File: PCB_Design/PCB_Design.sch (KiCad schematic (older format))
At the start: 14 parts

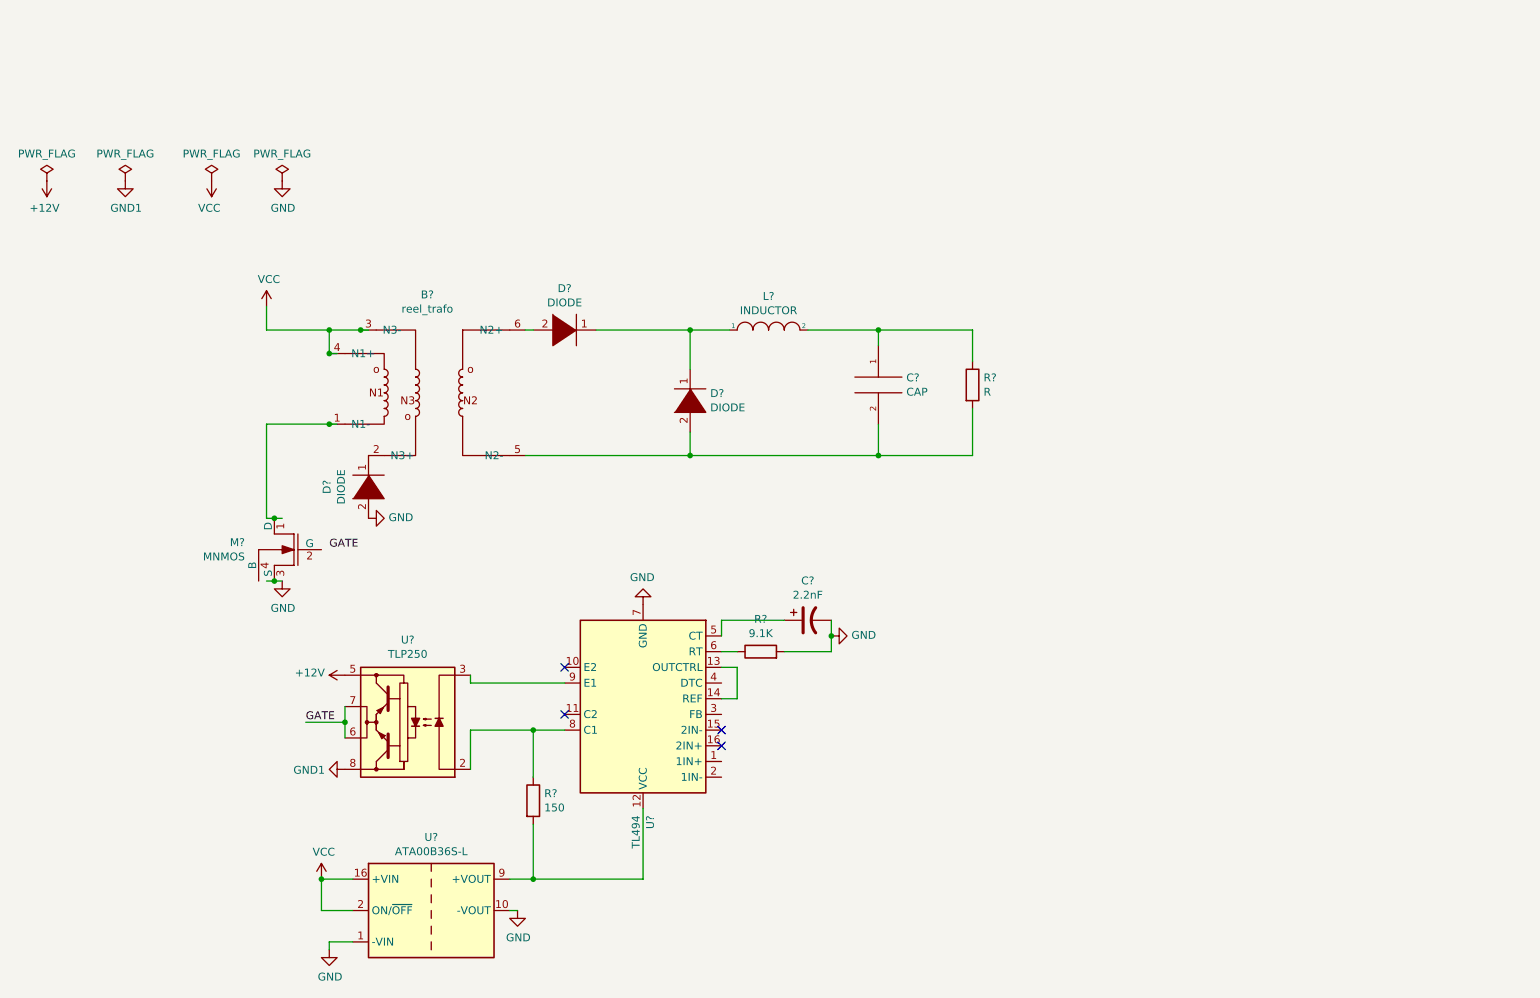
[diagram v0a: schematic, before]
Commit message: schematic and footprint assoc are done
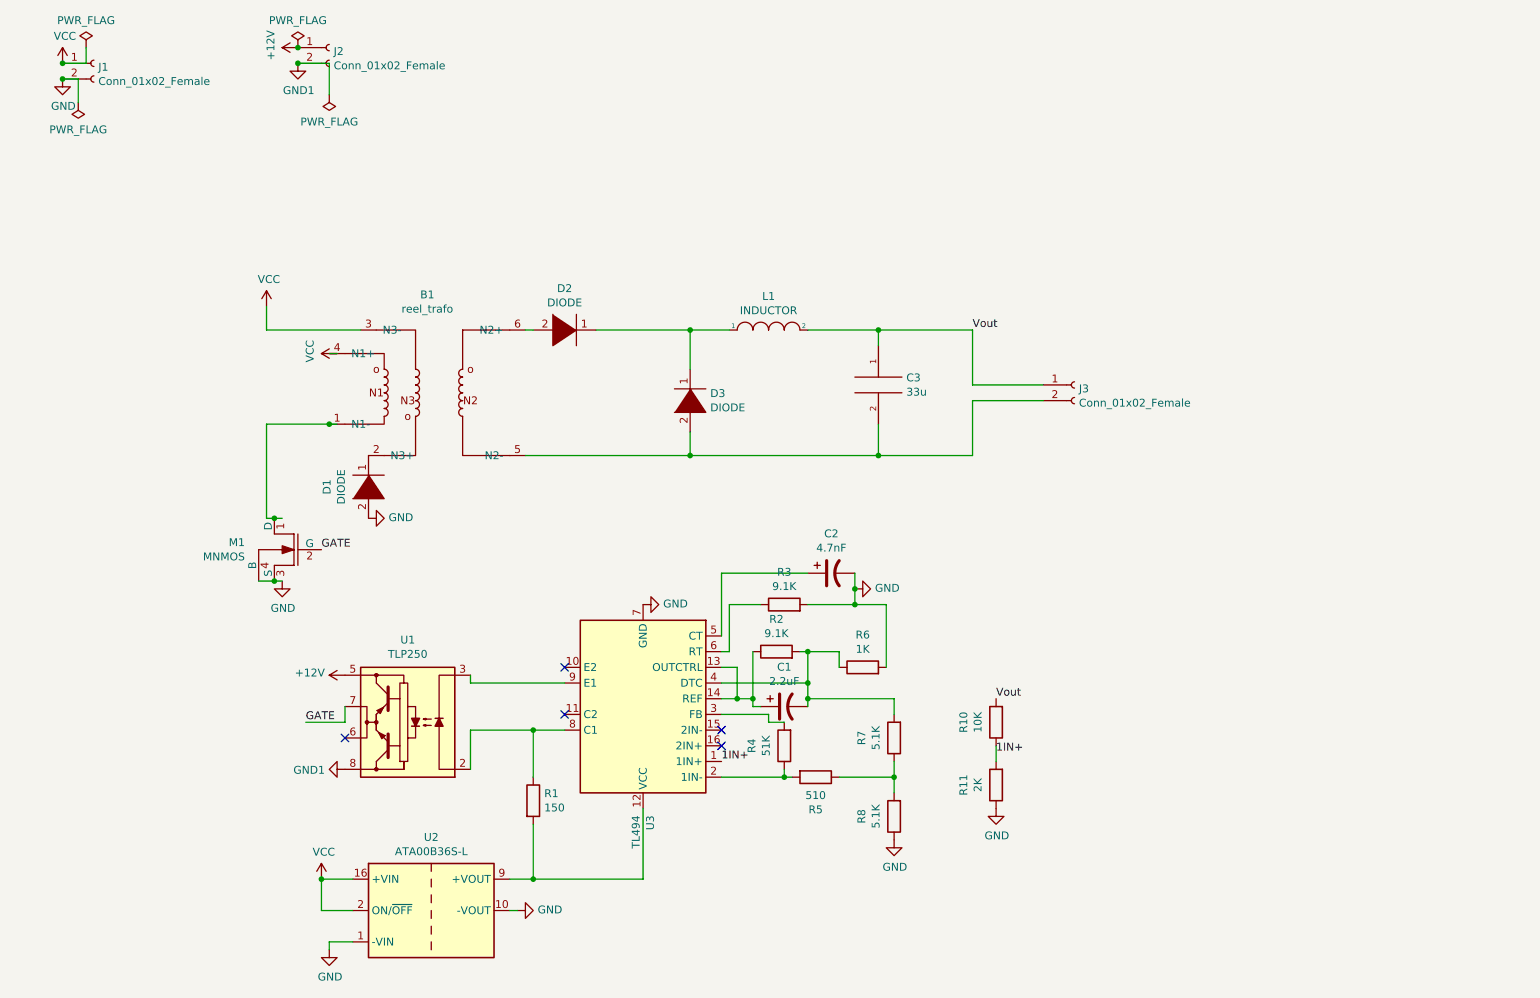
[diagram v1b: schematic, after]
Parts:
- removed R?: R, symbol Device:R
- added C1: 2.2uF, symbol Device:CP1
- added J1, J2, J3: Conn_01x02_Female, symbol Connector:Conn_01x02_Female
- added R10: 10K, Resistor_SMD:R_2512_6332Metric, symbol Device:R
- added R11: 2K, Resistor_SMD:R_2512_6332Metric, symbol Device:R
- added R2: 9.1K, Resistor_SMD:R_2512_6332Metric, symbol Device:R
- added R4: 51K, Resistor_SMD:R_2512_6332Metric, symbol Device:R
- added R5: 510, Resistor_SMD:R_2512_6332Metric, symbol Device:R
- added R6: 1K, Resistor_SMD:R_2512_6332Metric, symbol Device:R
- added R7, R8: 5.1K, Resistor_SMD:R_2512_6332Metric, symbol Device:R
- C2: renamed from C?; value 2.2nF -> 4.7nF
- C3: renamed from C?; value CAP -> 33u; footprint (none) -> Capacitor_SMD:C_1206_3216Metric_Pad1.42x1.75mm_HandSolder
- R1, R3: renamed from R?; footprint (none) -> Resistor_SMD:R_2512_6332Metric
- U3: renamed from U?; footprint (none) -> Package_DIP:DIP-16_W7.62mm
- gave numbers to parts that had none: 8
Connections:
- net labels added: 1IN+, Vout
- wire segments 55 -> 86
- no-connect marks 4 -> 5
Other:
- moved on the sheet: C2, R3

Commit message: started layout
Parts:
- removed J3: Conn_01x02_Female, symbol Connector:Conn_01x02_Female
- added J3: Conn_01x02_Male, Connector:Banana_Jack_2Pin, symbol Connector:Conn_01x02_Male
- B1: footprint (none) -> Transformer_THT:trafo
- C1, C2: footprint (none) -> Capacitor_SMD:C_1206_3216Metric_Pad1.42x1.75mm_HandSolder
- D1, D2, D3: footprint (none) -> Package_TO_SOT_THT:TO-220-2_Vertical
- J1, J2: footprint (none) -> Connector:Banana_Jack_2Pin
- L1: footprint (none) -> Inductor_THT:L_Toroid_Horizontal_D32.5mm_P28.90mm_Bourns_2300
- M1: footprint (none) -> Package_TO_SOT_THT:TO-220-3_Vertical
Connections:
- net Vout: now also J3.2 (Pin_2)
- net at B1.5 (N2-), C3.2, D3.2 (K): now also J3.1 (Pin_1)
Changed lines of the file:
@@
 F 0 "D1" H 3300 4065 50  0000 C CNN
 F 1 "DIODE" H 3300 3974 50  0000 C CNN
-F 2 "" H 3300 3800 50  0001 C CNN
+F 2 "Package_TO_SOT_THT:TO-220-2_Vertical" H 3300 3800 50  0001 C CNN
 F 3 "~" H 3300 3800 50  0001 C CNN
 	1    3300 3800
@@
 F 0 "D2" H 4550 3065 50  0000 C CNN
 F 1 "DIODE" H 4550 2974 50  0000 C CNN
-F 2 "" H 4550 2800 50  0001 C CNN
+F 2 "Package_TO_SOT_THT:TO-220-2_Vertical" H 4550 2800 50  0001 C CNN
 F 3 "~" H 4550 2800 50  0001 C CNN
 	1    4550 2800
@@
 F 0 "D3" V 5396 3122 50  0000 R CNN
 F 1 "DIODE" V 5305 3122 50  0000 R CNN
-F 2 "" H 5350 3250 50  0001 C CNN
+F 2 "Package_TO_SOT_THT:TO-220-2_Vertical" H 5350 3250 50  0001 C CNN
 F 3 "~" H 5350 3250 50  0001 C CNN
 	1    5350 3250
@@
 F 0 "L1" H 5850 3015 50  0000 C CNN
 F 1 "INDUCTOR" H 5850 2924 50  0000 C CNN
-F 2 "" H 5850 2800 50  0001 C CNN
+F 2 "Inductor_THT:L_Toroid_Horizontal_D32.5mm_P28.90mm_Bourns_2300" H 5850 2800 50  0001 C CNN
 F 3 "~" H 5850 2800 50  0001 C CNN
 	1    5850 2800
@@
 F 0 "M1" H 3088 4246 50  0000 L CNN
 F 1 "MNMOS" H 3088 4155 50  0000 L CNN
-F 2 "" H 2775 4200 50  0001 C CNN
+F 2 "Package_TO_SOT_THT:TO-220-3_Vertical" H 2775 4200 50  0001 C CNN
 F 3 "~" H 2775 4200 50  0001 C CNN
 	1    2800 4200
@@
 F 0 "B1" H 3675 4225 50  0000 C CNN
 F 1 "reel_trafo" H 3675 4134 50  0000 C CNN
-F 2 "" H 3500 3250 50  0001 C CNN
+F 2 "Transformer_THT:trafo" H 3500 3250 50  0001 C CNN
 F 3 "" H 3500 3250 50  0001 C CNN
 	1    3650 3400
@@
 F 0 "C2" V 5998 4350 50  0000 C CNN
 F 1 "4.7nF" V 6089 4350 50  0000 C CNN
-F 2 "" H 6250 4350 50  0001 C CNN
+F 2 "Capacitor_SMD:C_1206_3216Metric_Pad1.42x1.75mm_HandSolder" H 6250 4350 50  0001 C CNN
 F 3 "~" H 6250 4350 50  0001 C CNN
 	1    6250 4350
@@
 F 0 "C1" V 5698 5200 50  0000 C CNN
 F 1 "2.2uF" V 5789 5200 50  0000 C CNN
-F 2 "" H 5950 5200 50  0001 C CNN
+F 2 "Capacitor_SMD:C_1206_3216Metric_Pad1.42x1.75mm_HandSolder" H 5950 5200 50  0001 C CNN
 F 3 "~" H 5950 5200 50  0001 C CNN
 	1    5950 5200
@@
 F 0 "J1" H 1578 1076 50  0000 L CNN
 F 1 "Conn_01x02_Female" H 1578 985 50  0000 L CNN
-F 2 "" H 1550 1100 50  0001 C CNN
+F 2 "Connector:Banana_Jack_2Pin" H 1550 1100 50  0001 C CNN
 F 3 "~" H 1550 1100 50  0001 C CNN
 	1    1550 1100
@@
 F 0 "J2" H 3078 976 50  0000 L CNN
 F 1 "Conn_01x02_Female" H 3078 885 50  0000 L CNN
-F 2 "" H 3050 1000 50  0001 C CNN
+F 2 "Connector:Banana_Jack_2Pin" H 3050 1000 50  0001 C CNN
 F 3 "~" H 3050 1000 50  0001 C CNN
 	1    3050 1000
@@
 	3050 1100 2850 1100
 Connection ~ 2850 1100
-$Comp
-L Connector:Conn_01x02_Female J3
-U 1 1 5EF2B054
-P 7800 3150
-F 0 "J3" H 7828 3126 50  0000 L CNN
-F 1 "Conn_01x02_Female" H 7828 3035 50  0000 L CNN
-F 2 "" H 7800 3150 50  0001 C CNN
-F 3 "~" H 7800 3150 50  0001 C CNN
-	1    7800 3150
-	1    0    0    -1
-$EndComp
 Wire Wire Line
 	7600 3150 7150 3150
@@
 Wire Wire Line
 	7150 3250 7150 3600
+$Comp
+L Connector:Conn_01x02_Male J3
+U 1 1 5EEC8F4E
+P 7800 3250
+F 0 "J3" H 7772 3132 50  0000 R CNN
+F 1 "Conn_01x02_Male" H 7772 3223 50  0000 R CNN
+F 2 "Connector:Banana_Jack_2Pin" H 7800 3250 50  0001 C CNN
+F 3 "~" H 7800 3250 50  0001 C CNN
+	1    7800 3250
+	-1   0    0    1
+$EndComp
 $EndSCHEMATC

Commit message: started pcb design, looking good for a newbie
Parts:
- removed M1: MNMOS, Package_TO_SOT_THT:TO-220-3_Vertical, symbol pspice:MNMOS
- removed R1: 150, Resistor_SMD:R_2512_6332Metric, symbol Device:R
- added Q1: Q_NMOS_DGS, Package_TO_SOT_THT:TO-220-3_Vertical, symbol Device:Q_NMOS_DGS
- D1: footprint Package_TO_SOT_THT:TO-220-2_Vertical -> Package_TO_SOT_THT:TO-220-2_Horizontal_TabDown
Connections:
- net GATE: now also Q1.2 (G)
- net GND: now also Q1.3 (S)
- net at B1.1 (N1-): now also Q1.1 (D)
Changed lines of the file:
@@
 F 0 "D1" H 3300 4065 50  0000 C CNN
 F 1 "DIODE" H 3300 3974 50  0000 C CNN
-F 2 "Package_TO_SOT_THT:TO-220-2_Vertical" H 3300 3800 50  0001 C CNN
+F 2 "Package_TO_SOT_THT:TO-220-2_Horizontal_TabDown" H 3300 3800 50  0001 C CNN
 F 3 "~" H 3300 3800 50  0001 C CNN
 	1    3300 3800
@@
 $EndComp
 Wire Wire Line
-	5350 2800 5600 2800
-Connection ~ 5350 2800
-Wire Wire Line
 	6100 2800 6550 2800
 Wire Wire Line
@@
 Wire Wire Line
 	5050 5850 5050 6300
-Wire Wire Line
-	5050 6300 4350 6300
 NoConn ~ 4550 4950
 NoConn ~ 4550 5250
@@
 Wire Wire Line
 	2650 2650 2650 2800
-$Comp
-L pspice:MNMOS M1
-U 1 1 5ED38925
-P 2800 4200
-F 0 "M1" H 3088 4246 50  0000 L CNN
-F 1 "MNMOS" H 3088 4155 50  0000 L CNN
-F 2 "Package_TO_SOT_THT:TO-220-3_Vertical" H 2775 4200 50  0001 C CNN
-F 3 "~" H 2775 4200 50  0001 C CNN
-	1    2800 4200
-	-1   0    0    -1
-$EndComp
 $Comp
 L power:GND #PWR0106
@@
 Wire Wire Line
 	2650 3400 2650 4000
-Wire Wire Line
-	2750 4000 2700 4000
 $Comp
 L power:VCC #PWR0107
@@
 Wire Wire Line
 	2900 5300 3150 5300
-Text Label 3000 4200 0    50   ~ 0
+Text Label 2450 4200 1    50   ~ 0
 GATE
 Wire Wire Line
@@
 	3950 5050 3950 5000
 Wire Wire Line
-	4550 5350 4350 5350
-Wire Wire Line
 	3950 5350 3950 5600
-Connection ~ 2700 4000
-Wire Wire Line
-	2700 4000 2650 4000
 Connection ~ 3050 3400
 Wire Wire Line
@@
 Wire Wire Line
 	4350 2800 4300 2800
-$Comp
-L Device:R R1
-U 1 1 5EEECF4C
-P 4350 5800
-F 0 "R1" H 4420 5846 50  0000 L CNN
-F 1 "150" H 4420 5755 50  0000 L CNN
-F 2 "Resistor_SMD:R_2512_6332Metric" V 4280 5800 50  0001 C CNN
-F 3 "~" H 4350 5800 50  0001 C CNN
-	1    4350 5800
-	1    0    0    -1
-$EndComp
-Wire Wire Line
-	4350 5650 4350 5350
-Connection ~ 4350 5350
-Wire Wire Line
-	4350 5350 3950 5350
-Wire Wire Line
-	4350 5950 4350 6300
-Connection ~ 4350 6300
-Wire Wire Line
-	4350 6300 4200 6300
 $Comp
 L Device:CP1 C2
@@
 Wire Wire Line
 	5950 5650 5550 5650
-Wire Wire Line
-	2600 4400 2700 4400
-Wire Wire Line
-	2750 4400 2700 4400
-Connection ~ 2700 4400
 $Comp
 L Connector:Conn_01x02_Female J1
@@
 NoConn ~ 3150 5400
 Wire Wire Line
-	1500 1000 1500 1100
-Wire Wire Line
 	1500 1100 1350 1100
 Connection ~ 1350 1100
-Wire Wire Line
-	1450 1350 1450 1200
 Wire Wire Line
 	1450 1200 1350 1200
@@
 	-1   0    0    1
 $EndComp
+Wire Wire Line
+	5600 2800 5350 2800
+Connection ~ 5350 2800
+Wire Wire Line
+	1500 1000 1500 1100
+Wire Wire Line
+	1450 1200 1450 1350
+Wire Wire Line
+	2650 4000 2750 4000
+$Comp
+L Device:Q_NMOS_DGS Q1
+U 1 1 5EF1F730
+P 2650 4200
+F 0 "Q1" H 2854 4246 50  0000 L CNN
+F 1 "Q_NMOS_DGS" H 2854 4155 50  0000 L CNN
+F 2 "Package_TO_SOT_THT:TO-220-3_Vertical" H 2850 4300 50  0001 C CNN
+F 3 "~" H 2650 4200 50  0001 C CNN
+	1    2650 4200
+	1    0    0    -1
+$EndComp
+Wire Wire Line
+	3950 5350 4550 5350
+Wire Wire Line
+	4200 6300 5050 6300
 $EndSCHEMATC

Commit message: pcb design completed
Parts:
- added R1: 150, Resistor_THT:R_Axial_DIN0309_L9.0mm_D3.2mm_P12.70mm_Horizontal, symbol Device:R
- added R12: 4K, Resistor_THT:R_Axial_DIN0309_L9.0mm_D3.2mm_P12.70mm_Horizontal, symbol Device:R
- added R13: 1K, Resistor_THT:R_Axial_DIN0309_L9.0mm_D3.2mm_P12.70mm_Horizontal, symbol Device:R
- added R9: 0.2, Resistor_THT:R_Axial_DIN0309_L9.0mm_D3.2mm_P12.70mm_Horizontal, symbol Device:R
- R10, R11, R2, R3, R4, R5, R6, R7, R8: footprint Resistor_SMD:R_2512_6332Metric -> Resistor_THT:R_Axial_DIN0309_L9.0mm_D3.2mm_P12.70mm_Horizontal
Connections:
- net GND: now also R13.2, R9.1
- net at U2.9 (+VOUT), U3.12 (VCC): now also R1.2
- net REF: now reaches C1.1, R2.1, U3.13 (OUTCTRL), U3.14 (REF)
- net REF: now also R12.1
- net 2IN-: now reaches U3.15 (2IN-)
- net 2IN-: now also R12.2, R13.1
- net 2IN+: now reaches U3.16 (2IN+)
- net 2IN+: now also B1.5 (N2-), C3.2, D3.2 (K), J3.1 (Pin_1), R9.2
- net at U1.2 (A), U3.8 (C1): now also R1.1
- no-connect marks 5 -> 3
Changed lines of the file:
@@
 $EndComp
-$Comp
-L pspice:DIODE D3
-U 1 1 5ED3E515
-P 5350 3250
-F 0 "D3" V 5396 3122 50  0000 R CNN
-F 1 "DIODE" V 5305 3122 50  0000 R CNN
-F 2 "Package_TO_SOT_THT:TO-220-2_Vertical" H 5350 3250 50  0001 C CNN
-F 3 "~" H 5350 3250 50  0001 C CNN
-	1    5350 3250
-	0    -1   -1   0
-$EndComp
-Wire Wire Line
-	4750 2800 5350 2800
-Wire Wire Line
-	5350 2800 5350 3050
-Wire Wire Line
-	5350 3600 5350 3450
 $Comp
 L pspice:INDUCTOR L1
@@
 Wire Wire Line
 	5050 5850 5050 6300
-NoConn ~ 4550 4950
-NoConn ~ 4550 5250
-NoConn ~ 5550 5350
-NoConn ~ 5550 5450
 Wire Wire Line
 	2650 2650 2650 2800
@@
 GATE
 Wire Wire Line
-	4550 5050 3950 5050
-Wire Wire Line
-	3950 5050 3950 5000
-Wire Wire Line
 	3950 5350 3950 5600
 Connection ~ 3050 3400
@@
 F 0 "R3" V 6157 4550 50  0000 C CNN
 F 1 "9.1K" V 6066 4550 50  0000 C CNN
-F 2 "Resistor_SMD:R_2512_6332Metric" V 5880 4550 50  0001 C CNN
+F 2 "Resistor_THT:R_Axial_DIN0309_L9.0mm_D3.2mm_P12.70mm_Horizontal" V 5880 4550 50  0001 C CNN
 F 3 "~" H 5950 4550 50  0001 C CNN
 	1    5950 4550
@@
 	6400 4450 6400 4350
 Wire Wire Line
-	5550 4950 5650 4950
-Wire Wire Line
-	5650 4950 5650 5150
-Wire Wire Line
-	5650 5150 5550 5150
-Wire Wire Line
 	5550 4350 5550 4750
 Wire Wire Line
@@
 F 0 "R2" V 6107 4850 50  0000 C CNN
 F 1 "9.1K" V 6016 4850 50  0000 C CNN
-F 2 "Resistor_SMD:R_2512_6332Metric" V 5830 4850 50  0001 C CNN
+F 2 "Resistor_THT:R_Axial_DIN0309_L9.0mm_D3.2mm_P12.70mm_Horizontal" V 5830 4850 50  0001 C CNN
 F 3 "~" H 5900 4850 50  0001 C CNN
 	1    5900 4850
@@
 F 0 "R6" V 6657 4950 50  0000 C CNN
 F 1 "1K" V 6566 4950 50  0000 C CNN
-F 2 "Resistor_SMD:R_2512_6332Metric" V 6380 4950 50  0001 C CNN
+F 2 "Resistor_THT:R_Axial_DIN0309_L9.0mm_D3.2mm_P12.70mm_Horizontal" V 6380 4950 50  0001 C CNN
 F 3 "~" H 6450 4950 50  0001 C CNN
 	1    6450 4950
@@
 Wire Wire Line
 	5750 5200 5800 5200
-Wire Wire Line
-	5750 5150 5650 5150
 Connection ~ 5750 5150
 Wire Wire Line
 	5750 5150 5750 5200
-Connection ~ 5650 5150
 Wire Wire Line
 	6100 4850 6100 5050
@@
 F 0 "R10" V 7507 5300 50  0000 C CNN
 F 1 "10K" V 7416 5300 50  0000 C CNN
-F 2 "Resistor_SMD:R_2512_6332Metric" V 7230 5300 50  0001 C CNN
+F 2 "Resistor_THT:R_Axial_DIN0309_L9.0mm_D3.2mm_P12.70mm_Horizontal" V 7230 5300 50  0001 C CNN
 F 3 "~" H 7300 5300 50  0001 C CNN
 	1    7300 5300
@@
 F 0 "R11" V 7507 5700 50  0000 C CNN
 F 1 "2K" V 7416 5700 50  0000 C CNN
-F 2 "Resistor_SMD:R_2512_6332Metric" V 7230 5700 50  0001 C CNN
+F 2 "Resistor_THT:R_Axial_DIN0309_L9.0mm_D3.2mm_P12.70mm_Horizontal" V 7230 5700 50  0001 C CNN
 F 3 "~" H 7300 5700 50  0001 C CNN
 	1    7300 5700
@@
 F 0 "R7" V 6857 5400 50  0000 C CNN
 F 1 "5.1K" V 6766 5400 50  0000 C CNN
-F 2 "Resistor_SMD:R_2512_6332Metric" V 6580 5400 50  0001 C CNN
+F 2 "Resistor_THT:R_Axial_DIN0309_L9.0mm_D3.2mm_P12.70mm_Horizontal" V 6580 5400 50  0001 C CNN
 F 3 "~" H 6650 5400 50  0001 C CNN
 	1    6650 5400
@@
 F 0 "R8" V 6857 5900 50  0000 C CNN
 F 1 "5.1K" V 6766 5900 50  0000 C CNN
-F 2 "Resistor_SMD:R_2512_6332Metric" V 6580 5900 50  0001 C CNN
+F 2 "Resistor_THT:R_Axial_DIN0309_L9.0mm_D3.2mm_P12.70mm_Horizontal" V 6580 5900 50  0001 C CNN
 F 3 "~" H 6650 5900 50  0001 C CNN
 	1    6650 5900
@@
 F 0 "R5" V 6357 5650 50  0000 C CNN
 F 1 "510" V 6266 5650 50  0000 C CNN
-F 2 "Resistor_SMD:R_2512_6332Metric" V 6080 5650 50  0001 C CNN
+F 2 "Resistor_THT:R_Axial_DIN0309_L9.0mm_D3.2mm_P12.70mm_Horizontal" V 6080 5650 50  0001 C CNN
 F 3 "~" H 6150 5650 50  0001 C CNN
 	1    6150 5650
@@
 F 0 "R4" V 6157 5450 50  0000 C CNN
 F 1 "51K" V 6066 5450 50  0000 C CNN
-F 2 "Resistor_SMD:R_2512_6332Metric" V 5880 5450 50  0001 C CNN
+F 2 "Resistor_THT:R_Axial_DIN0309_L9.0mm_D3.2mm_P12.70mm_Horizontal" V 5880 5450 50  0001 C CNN
 F 3 "~" H 5950 5450 50  0001 C CNN
 	1    5950 5450
@@
 $EndComp
 Wire Wire Line
-	5600 2800 5350 2800
-Connection ~ 5350 2800
-Wire Wire Line
 	1500 1000 1500 1100
 Wire Wire Line
@@
 $EndComp
 Wire Wire Line
-	3950 5350 4550 5350
-Wire Wire Line
-	4200 6300 5050 6300
+	3950 5350 4400 5350
+Wire Wire Line
+	4200 6300 4400 6300
+$Comp
+L Device:R R1
+U 1 1 5EED3DDD
+P 4400 5850
+F 0 "R1" H 4470 5896 50  0000 L CNN
+F 1 "150" H 4470 5805 50  0000 L CNN
+F 2 "Resistor_THT:R_Axial_DIN0309_L9.0mm_D3.2mm_P12.70mm_Horizontal" V 4330 5850 50  0001 C CNN
+F 3 "~" H 4400 5850 50  0001 C CNN
+	1    4400 5850
+	1    0    0    -1
+$EndComp
+Wire Wire Line
+	4400 5350 4400 5700
+Wire Wire Line
+	4400 6000 4400 6300
+Connection ~ 4400 6300
+Wire Wire Line
+	4400 6300 5050 6300
+Wire Wire Line
+	5350 3400 5350 3600
+Wire Wire Line
+	4750 2800 5350 2800
+$Comp
+L pspice:DIODE D3
+U 1 1 5EEE2441
+P 5350 3200
+F 0 "D3" V 5396 3072 50  0000 R CNN
+F 1 "DIODE" V 5305 3072 50  0000 R CNN
+F 2 "Package_TO_SOT_THT:TO-220-2_Vertical" H 5350 3200 50  0001 C CNN
+F 3 "~" H 5350 3200 50  0001 C CNN
+	1    5350 3200
+	0    -1   -1   0
+$EndComp
+Wire Wire Line
+	5350 3000 5350 2800
+Connection ~ 5350 2800
+Wire Wire Line
+	5350 2800 5600 2800
+Text Label 5550 5150 0    50   ~ 0
+REF
+Wire Wire Line
+	5550 5150 5750 5150
+Text Label 5550 4950 0    50   ~ 0
+REF
+Text Label 7850 5150 0    50   ~ 0
+REF
+$Comp
+L Device:R R12
+U 1 1 5EF0B39B
+P 7850 5300
+F 0 "R12" H 7920 5346 50  0000 L CNN
+F 1 "4K" H 7920 5255 50  0000 L CNN
+F 2 "Resistor_THT:R_Axial_DIN0309_L9.0mm_D3.2mm_P12.70mm_Horizontal" V 7780 5300 50  0001 C CNN
+F 3 "~" H 7850 5300 50  0001 C CNN
+	1    7850 5300
+	1    0    0    -1
+$EndComp
+$Comp
+L Device:R R13
+U 1 1 5EF0B95F
+P 7850 5700
+F 0 "R13" H 7920 5746 50  0000 L CNN
+F 1 "1K" H 7920 5655 50  0000 L CNN
+F 2 "Resistor_THT:R_Axial_DIN0309_L9.0mm_D3.2mm_P12.70mm_Horizontal" V 7780 5700 50  0001 C CNN
+F 3 "~" H 7850 5700 50  0001 C CNN
+	1    7850 5700
+	1    0    0    -1
+$EndComp
+$Comp
+L power:GND #PWR02
+U 1 1 5EF0BE8A
+P 7850 5850
+F 0 "#PWR02" H 7850 5600 50  0001 C CNN
+F 1 "GND" H 7855 5677 50  0000 C CNN
+F 2 "" H 7850 5850 50  0001 C CNN
+F 3 "" H 7850 5850 50  0001 C CNN
+	1    7850 5850
+	1    0    0    -1
+$EndComp
+Wire Wire Line
+	7850 5450 7850 5550
+Text Label 7850 5500 0    50   ~ 0
+2IN-
+Text Label 5550 5350 0    50   ~ 0
+2IN-
+$Comp
+L Device:R R9
+U 1 1 5EF16E5C
+P 7150 3850
+F 0 "R9" V 7357 3850 50  0000 C CNN
+F 1 "0.2" V 7266 3850 50  0000 C CNN
+F 2 "Resistor_THT:R_Axial_DIN0309_L9.0mm_D3.2mm_P12.70mm_Horizontal" V 7080 3850 50  0001 C CNN
+F 3 "~" H 7150 3850 50  0001 C CNN
+	1    7150 3850
+	-1   0    0    1
+$EndComp
+$Comp
+L power:GND #PWR01
+U 1 1 5EF17229
+P 7150 4000
+F 0 "#PWR01" H 7150 3750 50  0001 C CNN
+F 1 "GND" V 7155 3872 50  0000 R CNN
+F 2 "" H 7150 4000 50  0001 C CNN
+F 3 "" H 7150 4000 50  0001 C CNN
+	1    7150 4000
+	1    0    0    -1
+$EndComp
+Wire Wire Line
+	7150 3600 7150 3700
+Connection ~ 7150 3600
+Text Label 7150 3700 0    50   ~ 0
+2IN+
+Text Label 5550 5450 0    50   ~ 0
+2IN+
+Wire Wire Line
+	4550 5350 4400 5350
+Connection ~ 4400 5350
+Wire Wire Line
+	4550 5050 3950 5050
+Wire Wire Line
+	3950 5050 3950 5000
+NoConn ~ 4550 5250
+NoConn ~ 4550 4950
 $EndSCHEMATC
